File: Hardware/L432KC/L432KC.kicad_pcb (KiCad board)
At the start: 2 copper layers, 74.9 x 55.9 mm, 44 parts, among them J1 L4_G4, J2 USB_B_Micro, J3 JTAG, J4 3v3, J5 GND, J6 Conn_01x07, J7 Conn_01x07_Male, J8 TVCC, J9 LogicAna, U1 AD8531ARTZ, U2 SRV05-4, U3 NUCLEO-L432KC, U4 TXB0304RUT, U5 TXB0304RUT, U6 74LVC1G125

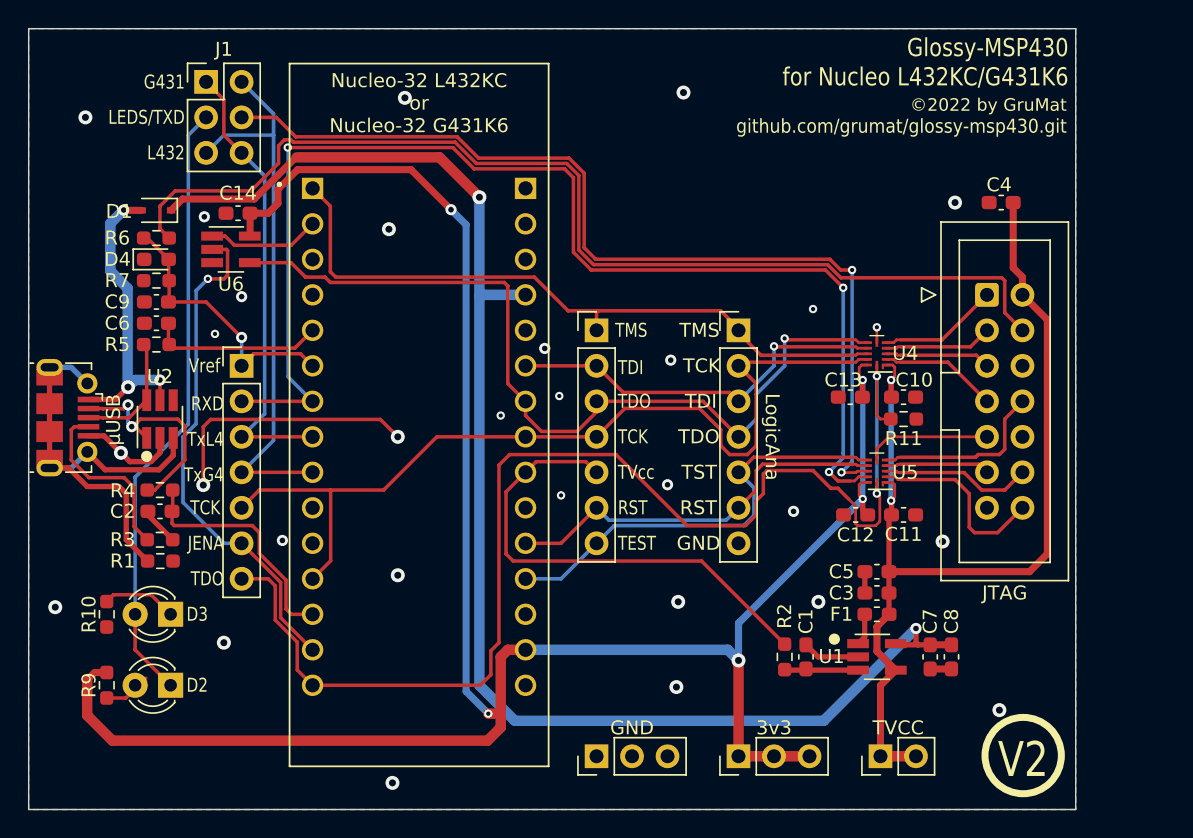
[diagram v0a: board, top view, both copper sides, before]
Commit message: Updated L432KC/G431K6 prototype board.
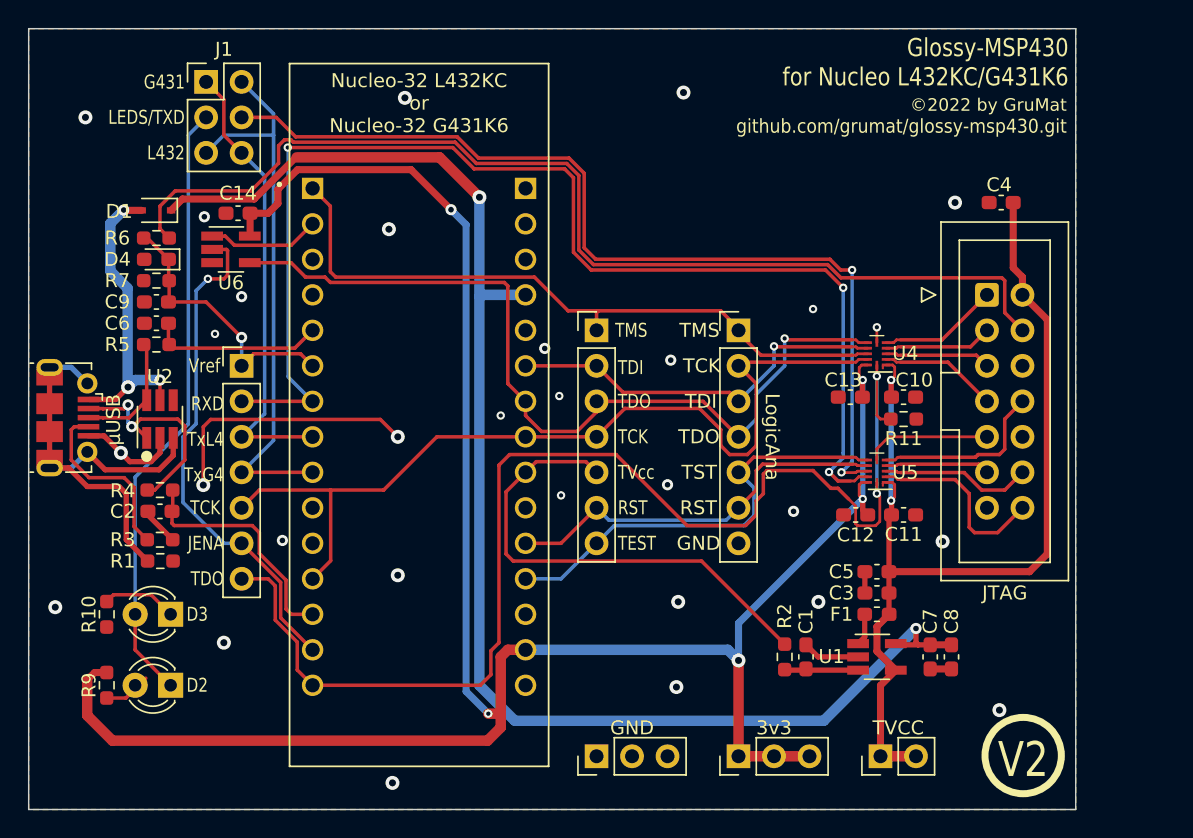
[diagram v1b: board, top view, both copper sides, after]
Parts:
- U6: value 74LVC1G125 -> SN74LVC1G125
- turned D4 to 180 degrees
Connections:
- net VDC renamed VCC
- D4 pad 1: GND -> /VREF_2
- D4 pad 2: /VREF_2 -> GND

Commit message: Updated L432KC prototype to use low impedance output buffers for voltage translation.
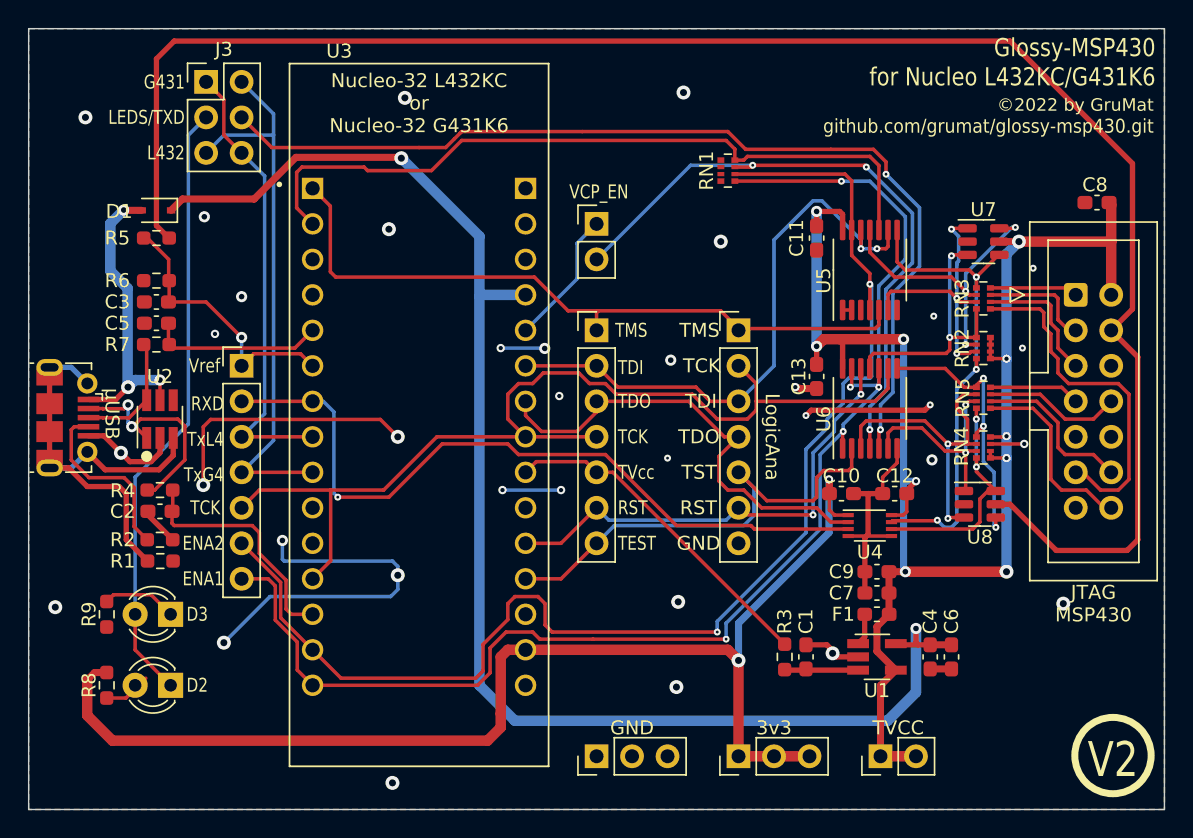
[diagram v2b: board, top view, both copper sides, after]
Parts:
- removed C14: 100nF, Capacitor_SMD:C_0603_1608Metric_Pad1.08x0.95mm_HandSolder
- removed D4: 82356050050, Diode_SMD:D_0603_1608Metric_Pad1.05x0.95mm_HandSolder
- removed R11: 47K, Resistor_SMD:R_0603_1608Metric_Pad0.98x0.95mm_HandSolder
- added J4: VCP, Connector_PinHeader_2.54mm:PinHeader_1x02_P2.54mm_Vertical, F.Cu at (142.2, 88.9)
- added RN1: 47k, Resistor_SMD:R_Array_Convex_4x0402, F.Cu at (151.6, 85.1)
- added RN2: 47k, Resistor_SMD:R_Array_Convex_4x0402, F.Cu at (169.9, 97.8)
- added RN3: 47, Resistor_SMD:R_Array_Convex_4x0402, F.Cu at (169.9, 94.2)
- added RN4: 47k, Resistor_SMD:R_Array_Convex_4x0402, F.Cu at (169.9, 104.9)
- added RN5: 47, Resistor_SMD:R_Array_Convex_4x0402, F.Cu at (169.9, 101.3)
- added U7: SRV05-4, Package_TO_SOT_SMD:SOT-23-6, F.Cu at (169.9, 90.2)
- added U8: SRV05-4, Package_TO_SOT_SMD:SOT-23-6, F.Cu at (169.7, 109.0)
- U4: value TXB0304RUT -> SN74LVC2T45; footprint Package_DFN_QFN:Texas_R_PUQFN-N12 -> Package_SO:VSSOP-8_2.3x2mm_P0.5mm
- U5: value TXB0304RUT -> SN74LVC126A; footprint Package_DFN_QFN:Texas_R_PUQFN-N12 -> Package_SO:TSSOP-14_4.4x5mm_P0.65mm
- U6: value SN74LVC1G125 -> SN74LVC126A; footprint Package_TO_SOT_SMD:SOT-23-5_HandSoldering -> Package_SO:TSSOP-14_4.4x5mm_P0.65mm
- moved U6 47.1 mm to (161.8, 102.1), turned to 90 degrees
- moved C11 20.8 mm to (158.0, 89.9), turned to 90 degrees
- moved U5 14.4 mm to (161.8, 92.2), turned to 90 degrees
- moved U4 12.3 mm to (161.8, 110.5), turned to 0 degrees
- moved C10 8.21 mm to (159.8, 108.2), turned to 180 degrees
- moved C8 6.86 mm to (178.1, 87.4)
- moved J2 6.35 mm to (176.5, 94.0)
- moved C12 3.18 mm to (163.6, 108.2), turned to 0 degrees
- moved C13 2.83 mm to (158.0, 99.8), turned to 90 degrees
- renumbered C9 to C3, C7 to C4, C6 to C5, C8 to C6, C3 to C7, C4 to C8, C5 to C9, J2 to J1, J9 to J10, J3 to J2, J1 to J3, J4 to J5, J5 to J6, J6 to J7, J7 to J8, J8 to J9, R3 to R2, R2 to R3, R6 to R5, R7 to R6, R5 to R7, R9 to R8, R10 to R9
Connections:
- C10 pad 1: VCC -> GND
- C10 pad 2: GND -> +3V3
- C11 pad 1: VCC -> GND
- C11 pad 2: GND -> VCC
- C12 pad 1: +3.3V -> GND
- C12 pad 2: GND -> VCC
- C13 pad 1: +3.3V -> GND
- C13 pad 2: GND -> VCC
- J5 pad 1: +3.3V -> +3V3
- J5 pad 2: +3.3V -> +3V3
- J5 pad 3: +3.3V -> +3V3
- J7 pad 6: /SBW_OUT -> /ENA2
- J7 pad 7: /JENA -> /ENA1
- R8 pad 2: +3.3V -> +3V3
- U3 pad CN3_14: /SBW_OUT -> /ENA2
- U3 pad CN3_15: /JENA -> /ENA1
- U3 pad CN3_2: /SBW_DIR -> /SBWO
- U3 pad CN4_14: +3.3V -> +3V3
- U3 pad CN4_5: unconnected-(U3-PadCN4_5) -> /PA2
- U4 pad 1: VCC -> +3V3
- U4 pad 2: /JTCK -> /mTDO
- U4 pad 3: /JTMS -> /mRXD
- U4 pad 4: /JTDI -> GND
- U4 pad 5: /JTDO -> GND
- U4 pad 6: GND -> /rRXD
- U4 pad 7: /mTDO -> /rTDO
- U4 pad 8: /mTDI -> VCC
- U5 pad 1: VCC -> GND
- U5 pad 10: /mRXD -> /SBWO
- U5 pad 11: +3.3V -> /rTDI
- U5 pad 12: /JENA -> /mTDI
- U5 pad 2: /JRXD -> GND
- U5 pad 3: /JTXD -> unconnected-(U5-Pad3)
- U5 pad 4: /JRST -> /ENA2
- U5 pad 5: /JTEST -> /mTMS
- U5 pad 6: GND -> /rTMS
- U5 pad 7: /mTEST -> GND
- U5 pad 8: /mRST -> /rTDO
- U5 pad 9: /mTXD -> /mTDI
- U6 pad 1: /SBW_DIR -> /ENA1
- U6 pad 2: /SBW_OUT -> /mTEST
- U6 pad 3: GND -> /rTEST
- U6 pad 4: /mTDO -> /ENA3
- U6 pad 5: +3.3V -> /mTXD
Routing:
- net +3.3V: track 156.3 -> 0.00 mm, vias 5 -> 0
- net /ENA1: track 0.00 -> 98.1 mm, vias 0 -> 5
- net /ENA2: track 0.00 -> 94.4 mm, vias 0 -> 2
- net /JENA: track 90.4 -> 0.00 mm, vias 2 -> 0
- net +3V3: track 0.00 -> 88.8 mm, vias 0 -> 2
- net /SBWO: track 0.00 -> 53.0 mm
- net GND: track 46.1 -> 97.2 mm, vias 30 -> 35
- net /TVref: track 77.1 -> 127.4 mm
- net /ENA3: track 0.00 -> 46.2 mm, vias 0 -> 3
- net VCC: track 73.8 -> 114.6 mm, vias 2 -> 10
- net /SBW_OUT: track 36.3 -> 0.00 mm, vias 1 -> 0
- net /rTDO: track 0.00 -> 35.5 mm, vias 0 -> 3
- net /mRXD: track 87.8 -> 53.8 mm, vias 3 -> 1
- net /mTDO: track 61.5 -> 33.3 mm, vias 1 -> 0
- net /rTDI: track 0.00 -> 22.4 mm, vias 0 -> 3
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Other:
- board size 74.9 x 55.9 mm -> 81.3 x 55.9 mm
- board text added: "ENA1"
- board text added: "ENA2"
- board text added: "JTAG MSP430"
- board text added: "VCP_EN"
- board text removed: "JENA"
- board text removed: "JTAG"

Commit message: - Review of values on L432KC
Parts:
- RN3, RN5: value 47 -> 100
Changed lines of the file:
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@@
       (effects (font (size 1 1) (thickness 0.15)))
     )
-    (fp_text value "47" (at 0 2.1) (layer "F.Fab")
+    (fp_text value "100" (at 0 2.1) (layer "F.Fab")
       (effects (font (size 1 1) (thickness 0.15)))
     )
@@
       (effects (font (size 1 1) (thickness 0.15)))
     )
-    (fp_text value "47" (at 0 2.1) (layer "F.Fab")
+    (fp_text value "100" (at 0 2.1) (layer "F.Fab")
       (effects (font (size 1 1) (thickness 0.15)))
     )
@@
     )
     (fp_line (start -9.27 -25.145) (end 9.27 -25.145) (layer "F.SilkS") (width 0.127))
+    (fp_line (start -9.27 25.145) (end -9.27 -25.145) (layer "F.SilkS") (width 0.127))
     (fp_line (start 9.27 -25.145) (end 9.27 25.145) (layer "F.SilkS") (width 0.127))
-    (fp_line (start -9.27 25.145) (end -9.27 -25.145) (layer "F.SilkS") (width 0.127))
     (fp_line (start 9.27 25.145) (end -9.27 25.145) (layer "F.SilkS") (width 0.127))
     (fp_circle (center -10 -16.5) (end -9.9 -16.5) (layer "F.SilkS") (width 0.2) (fill none))
     (fp_line (start -9.52 -25.395) (end 9.52 -25.395) (layer "F.CrtYd") (width 0.05))
-    (fp_line (start 9.52 -25.395) (end 9.52 25.395) (layer "F.CrtYd") (width 0.05))
     (fp_line (start 9.52 25.395) (end -9.52 25.395) (layer "F.CrtYd") (width 0.05))
     (fp_line (start -9.52 25.395) (end -9.52 -25.395) (layer "F.CrtYd") (width 0.05))
+    (fp_line (start 9.52 -25.395) (end 9.52 25.395) (layer "F.CrtYd") (width 0.05))
+    (fp_line (start 9.27 -25.145) (end 9.27 25.145) (layer "F.Fab") (width 0.127))
     (fp_line (start 9.27 25.145) (end -9.27 25.145) (layer "F.Fab") (width 0.127))
+    (fp_line (start -9.27 -25.145) (end 9.27 -25.145) (layer "F.Fab") (width 0.127))
     (fp_line (start -9.27 25.145) (end -9.27 -25.145) (layer "F.Fab") (width 0.127))
-    (fp_line (start -9.27 -25.145) (end 9.27 -25.145) (layer "F.Fab") (width 0.127))
-    (fp_line (start 9.27 -25.145) (end 9.27 25.145) (layer "F.Fab") (width 0.127))
     (fp_circle (center -10 -16.5) (end -9.9 -16.5) (layer "F.Fab") (width 0.2) (fill none))
     (pad "CN3_1" thru_hole rect (at -7.62 -16.215) (size 1.53 1.53) (drill 1.02) (layers *.Cu *.Mask)

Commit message: Changed output buffer part#
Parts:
- U4: value SN74LVC2T45 -> 74AVCH2T45DC
- U5, U6: value SN74LVC126A -> 74LVC125APW
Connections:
- net /ENA1 renamed /ENA1N
- net /ENA2 renamed /ENA2N
- net /ENA3 renamed /ENA3N
